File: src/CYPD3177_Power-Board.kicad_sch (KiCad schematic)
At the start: 0 parts

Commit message: Add: Initialized schematic, used the Infineon-CY4533_Guide-UserManual as a guide
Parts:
- added C1, C2, C6, C7: 1µF, symbol Device:C
- added C10: 4.7nF, symbol Device:C
- added C3, C4: 0.1µF, symbol Device:C
- added C5: 3.3µF, symbol Device:C
- added C8, C9: 390pF, symbol Device:C
- added D1: NZH10C,115, symbol Device:D_Zener
- added D2: LTST-C190GKT, symbol Device:LED
- added D3: LED, symbol Device:LED
- added J1: Conn_01x06_Pin, symbol Connector:Conn_01x06_Pin
- added J2: USB4125-GF-A, Connectors_User:GCT_USB4125-GF-A, symbol Connector_User:USB4125-GF-A
- added J3: Conn_01x10_Pin, symbol Connector:Conn_01x10_Pin
- added Q1: IRF9358PbF, Package_SO:HSOP-8-1EP_3.9x4.9mm_P1.27mm_EP2.41x3.1mm_ThermalVias, symbol Transistor_FET_User:IRF9358PBF
- added Q2: BSL308PE, Package_TO_SOT_SMD:SOT-23-6_Handsoldering, symbol Transistor_FET_User:BSL308PE
- added Q3: NTR4503N, symbol Simulation_SPICE:NMOS
- added R1, R5: 49.9kΩ, symbol Device:R
- added R10, R11, R12, R9: 2kΩ, symbol Device:R
- added R13, R4, R7: 1kΩ, symbol Device:R
- added R14: 100kΩ, symbol Device:R
- added R15: 0kΩ, symbol Device:R
- added R16: 5.1Ω, symbol Device:R
- added R17, R19, R20, R21: 5.1kΩ, symbol Device:R
- added R18, R22, R3: 0Ω, symbol Device:R
- added R2: 10kΩ, symbol Device:R
- added R6: 2.2kΩ, symbol Device:R
- added R8: 1M, symbol Device:R
- added U1: CYPD3177-24LQXQx, Package_DFN_QFN:QFN-24-1EP_4x4mm_P0.5mm_EP2.7x2.7mm_ThermalVias, symbol Interface_USB_User:CYPD3177-24LQXQx
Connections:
- new net: Q2.1, Q2.3, R5.2, R7.1
- new net: R7.2, U1.4 (SAFE_PWR_EN)
- new net: J3.6 (Pin_6), R11.2, U1.7 (HPI_INT)
- new net: D2.2 (A), R6.2
- new net: R15.2, R16.1, U1.2 (VBUS_MAX)
- new net: C6.2, C7.2, R2.2, R3.2, R4.1
- new net: Q2.4, Q2.5
- new net: C10.1, J2.S1 (SHIELD), R8.1
- new net: R17.2, R18.1, U1.1 (VBUS_MIN)
- new net: J3.9 (Pin_9), R9.2, U1.10 (FLIP)
- new net: C9.1, J2.B5 (CC2), U1.14 (CC2)
- new net: Q3.1 (D), R13.2
- new net: J3.10 (Pin_10), Q3.2 (G), R14.1, U1.9 (FAULT)
- new net: C8.1, J2.A5 (CC1), U1.15 (CC1)
- new net: J3.5 (Pin_5), R12.2, U1.12 (HPI_SDA)
- new net: R19.2, R20.1, U1.5 (ISNK_COARSE)
- new net: D3.1 (K), R13.1
- new net: J3.4 (Pin_4), U1.13 (HPI_SCL)
- new net: R4.2, U1.3 (VBUS_FET_EN)
- new net: R21.2, R22.1, U1.6 (ISNK_FINE)
- new net: J3.7 (Pin_7), R10.2, U1.8 (GPIO_1)
- new net +1V8: C1.1, J3.2 (Pin_2), U1.24 (VCCD)
- new net +3V3: C2.1, C3.1, C4.1, J3.1 (Pin_1), R10.1, R11.1, R12.1, R15.1, R17.1, R19.1, R21.1, R9.1, U1.23 (VDDD)
- new net 5V_{OUT}: J1.3 (Pin_3), J1.4 (Pin_4), Q2.2
- new net DC_{OUT}: C7.1, D3.2 (A), J1.1 (Pin_1), J1.2 (Pin_2), J3.8 (Pin_8), Q1.3, U1.11 (VDC_OUT)
- new net FET_{Gate}: D1.2 (A), Q1.2, Q1.4, R1.2, R3.1
- new net FET_{SRC}: D1.1 (K), Q1.1, Q1.5, Q1.6, R1.1
- new net GND: C1.2, C10.2, C2.2, C3.2, C4.2, C5.2, C8.2, C9.2, D2.1 (K), J1.5 (Pin_5), J1.6 (Pin_6), J2.A12 (GND), J2.B12 (GND), J3.3 (Pin_3), Q3.3 (S), R14.2, R16.2, R18.2, R20.2, R22.2, R8.2, U1.19 (GND), U1.22 (VSS), U1.25 (EPAD)
- new net VBUS: C5.1, C6.1, J2.A9 (VBUS), J2.B9 (VBUS), Q1.7, Q1.8, Q2.6, R2.1, R5.1, R6.1, U1.18 (VBUS_IN)
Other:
- note added: "I_{Sink, Coarse}"
- note added: "I_{Sink, Fine}"
- note added: "VBUS_{MAX}"
- note added: "VBUS_{MIN}"
- title: <Default Template> -> CYPD3177_Power-Board

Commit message: Mod: Schematic, modified some resistor value to not use as much; Add: Description texts and tables
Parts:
- removed J3: Conn_01x10_Pin, symbol Connector:Conn_01x10_Pin
- added J3, J4, J5: Conn_01x03, symbol Connector_Generic:Conn_01x03
- R10, R11, R12, R9: value 2kΩ -> 2.2kΩ
- R15: value 0kΩ -> 5.1kΩ
- R18, R22: value 0Ω -> 2.2kΩ
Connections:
- net +1V8: now also J3.2 (Pin_2)
- net +3V3: now also J3.1 (Pin_1)
- net DC_{OUT}: no longer D3.2 (A)
- net GND: now also J3.3 (Pin_3)
- net VBUS: now also D3.2 (A)
- net ~{INT}: now reaches R11.2, U1.7 (HPI_INT)
- net ~{INT}: now also J4.3 (Pin_3)
- net VBUS_{MAX}: now reaches R15.2, R16.1, U1.2 (VBUS_MAX)
- net VBUS_{MIN}: now reaches R17.2, R18.1, U1.1 (VBUS_MIN)
- net FLIP: now reaches R9.2, U1.10 (FLIP)
- net FLIP: now also J5.2 (Pin_2)
- net CC2: now reaches C9.1, J2.B5 (CC2), U1.14 (CC2)
- net FAULT: now reaches Q3.2 (G), R14.1, U1.9 (FAULT)
- net FAULT: now also J5.3 (Pin_3)
- net CC1: now reaches C8.1, J2.A5 (CC1), U1.15 (CC1)
- net SDA: now reaches R12.2, U1.12 (HPI_SDA)
- net SDA: now also J4.2 (Pin_2)
- net I_{Sink, Coarse}: now reaches R19.2, R20.1, U1.5 (ISNK_COARSE)
- net SCL: now reaches U1.13 (HPI_SCL)
- net SCL: now also J4.1 (Pin_1)
- net I_{Sink, Fine}: now reaches R21.2, R22.1, U1.6 (ISNK_FINE)
- net GPIO: now reaches R10.2, U1.8 (GPIO_1)
- net GPIO: now also J5.1 (Pin_1)
- net 5V_{OUT} renamed Safe-5V_{OUT}
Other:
- note added: "* When pullup-pulldown combination is 0-none or none-0, use any resistor instead of 0-ohm"
- note added: "+3V3 Ratio"
- note added: "0.25A"
- note added: "0.5A"
- note added: "0.75A"
- note added: "0.9A"
- note added: "0/6"
- note added: "0A"
- note added: "0kΩ*"
- note added: "1/6"
- note added: "10kΩ"
- note added: "12V"
- note added: "15V"
- note added: "19V"
- note added: "1A"
- note added: "1kΩ"
- note added: "2.4kΩ"
- note added: "2/6"
- note added: "20V"
- note added: "2A"
- note added: "3/6"
- note added: "3A"
- note added: "4/6"
- note added: "4A"
- note added: "5.1kΩ"
- note added: "5A"
- note added: "5V"
- note added: "9V"
- note added: ">5/6"
- note added: "Coarse Current"
- note added: "Fine Current"
- note added: "Pull-Down"
- note added: "Pull-Up"
- note added: "Req. Voltage"
- note added: "open"
- moved on the sheet: D2, D3, Q3, R10, R13, R14, R9

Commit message: Mod: Power connector and changed date
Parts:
- removed J1: Conn_01x06_Pin, symbol Connector:Conn_01x06_Pin
- added J1: Conn_01x06, symbol Connector_Generic:Conn_01x06
- D3: value LED -> RED
- renumbered R15 to R14, R17 to R15, R19 to R16, R21 to R17, R14 to R18, R16 to R19, R18 to R20, R20 to R21
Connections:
- net DC_{OUT}: now also J1.1 (Pin_1), J1.2 (Pin_2)
- net GND: now also J1.5 (Pin_5), J1.6 (Pin_6)
- net Safe-5V_{OUT}: now also J1.3 (Pin_3), J1.4 (Pin_4)
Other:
- note added: "Clamp V_{GS} to 10V absolute"
- moved on the sheet: C5

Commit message: Mod: Assigned all footprints, without the connectors
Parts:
- added C5, C6: 1µF, Capacitor_SMD:C_0402_1005Metric, symbol Device:C
- C1, C2: footprint (none) -> Capacitor_SMD:C_0603_1608Metric
- C10: renamed from C8; footprint (none) -> Capacitor_SMD:C_0603_1608Metric_Pad1.08x0.95mm_HandSolder; now not fitted
- C11: renamed from C9; footprint (none) -> Capacitor_SMD:C_0603_1608Metric_Pad1.08x0.95mm_HandSolder; now not fitted
- C12: renamed from C10; footprint (none) -> Capacitor_SMD:C_0805_2012Metric_Pad1.18x1.45mm_HandSolder
- C3, C4: footprint (none) -> Capacitor_SMD:C_0402_1005Metric
- C7: renamed from C5; value 3.3µF -> 1µF; footprint (none) -> Capacitor_SMD:C_0402_1005Metric
- C8: renamed from C6; footprint (none) -> Capacitor_SMD:C_0402_1005Metric
- C9: renamed from C7; footprint (none) -> Capacitor_SMD:C_0402_1005Metric_Pad0.74x0.62mm_HandSolder; now not fitted
- D1: footprint (none) -> Diode_SMD:D_SOD-123F
- D2: footprint (none) -> LED_SMD:LED_0603_1608Metric_Pad1.05x0.95mm_HandSolder
- D3: value RED -> LTST-C190EKT; footprint (none) -> LED_SMD:LED_0603_1608Metric_Pad1.05x0.95mm_HandSolder
- Q3: footprint (none) -> Package_TO_SOT_SMD:SOT-23-3
- R1, R4, R5, R7: footprint (none) -> Resistor_SMD:R_0402_1005Metric
- R10, R11, R12, R14, R15, R16, R17, R19, R20, R21, R22, R6, R8, R9: footprint (none) -> Resistor_SMD:R_0805_2012Metric_Pad1.20x1.40mm_HandSolder
- R13, R3: footprint (none) -> Resistor_SMD:R_0402_1005Metric_Pad0.72x0.64mm_HandSolder
- R18: value 100kΩ -> 49.9kΩ; footprint (none) -> Resistor_SMD:R_0402_1005Metric_Pad0.72x0.64mm_HandSolder
- R2: footprint (none) -> Resistor_SMD:R_0603_1608Metric
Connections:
- net GND: now also C5.2, C6.2
- net VBUS: now also C5.1, C6.1
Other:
- moved on the sheet: C1, C2, C3, C4, D1, D3, Q3, R1, R13

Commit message: Add: Footprint for the connectors (castellated holes) and mounting holes
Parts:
- added H1, H2: MountingHole, MountingHole:MountingHole_3.2mm_M3, symbol Mechanical:MountingHole
- J1: footprint (none) -> Connector_CastellatedHole_2.54mm_User:CastellatedHole_1x06_P2.54mm_PinHeaders
- J2: footprint Connectors_User:GCT_USB4125-GF-A -> Connector_User:GCT_USB4125-GF-A
- J3, J4, J5: footprint (none) -> Connector_CastellatedHole_2.54mm_User:CastellatedHole_1x03_P2.54mm_PinHeader
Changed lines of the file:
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@@
       (effects (font (size 1.27 1.27)) (justify left))
     )
-    (property "Footprint" "" (at 266.7 121.92 0)
+    (property "Footprint" "Connector_CastellatedHole_2.54mm_User:CastellatedHole_1x03_P2.54mm_PinHeader" (at 266.7 121.92 0)
       (effects (font (size 1.27 1.27)) hide)
     )
@@
       (effects (font (size 1.27 1.27)))
     )
-    (property "Footprint" "Connectors_User:GCT_USB4125-GF-A" (at 50.8 80.01 0)
+    (property "Footprint" "Connector_User:GCT_USB4125-GF-A" (at 50.8 80.01 0)
       (effects (font (size 1.27 1.27)) hide)
     )
@@
       (effects (font (size 1.27 1.27)) (justify left))
     )
-    (property "Footprint" "" (at 266.7 111.76 0)
+    (property "Footprint" "Connector_CastellatedHole_2.54mm_User:CastellatedHole_1x03_P2.54mm_PinHeader" (at 266.7 111.76 0)
       (effects (font (size 1.27 1.27)) hide)
     )
@@
       (effects (font (size 1.27 1.27)) (justify left))
     )
-    (property "Footprint" "" (at 266.7 24.13 0)
+    (property "Footprint" "Connector_CastellatedHole_2.54mm_User:CastellatedHole_1x06_P2.54mm_PinHeaders" (at 266.7 24.13 0)
       (effects (font (size 1.27 1.27)) hide)
     )
@@
   (symbol (lib_id "power:GND") (at 72.39 87.63 0) (unit 1)
     (in_bom yes) (on_board yes) (dnp no) (fields_autoplaced)
-    (property "Reference" "#PWR09" (at 72.39 93.98 0)
+    (property "Reference" "#PWR010" (at 72.39 93.98 0)
       (effects (font (size 1.27 1.27)) hide)
     )
@@
       (project "CYPD3177_Power-Board"
         (path "/bfaac094-0365-40a4-8b7a-d4d62ace544e"
-          (reference "#PWR09") (unit 1)
+          (reference "#PWR010") (unit 1)
         )
       )
@@
       (effects (font (size 1.27 1.27)) (justify left))
     )
-    (property "Footprint" "" (at 266.7 88.9 0)
+    (property "Footprint" "Connector_CastellatedHole_2.54mm_User:CastellatedHole_1x03_P2.54mm_PinHeader" (at 266.7 88.9 0)
       (effects (font (size 1.27 1.27)) hide)
     )
@@
     )
   )
+  (symbol (lib_id "Mechanical:MountingHole") (at 25.4 190.5 0) (unit 1)
+    (in_bom yes) (on_board yes) (dnp no) (fields_autoplaced)
+    (property "Reference" "H2" (at 27.94 189.865 0)
+      (effects (font (size 1.27 1.27)) (justify left))
+    )
+    (property "Value" "MountingHole" (at 27.94 192.405 0)
+      (effects (font (size 1.27 1.27)) (justify left))
+    )
+    (property "Footprint" "MountingHole:MountingHole_3.2mm_M3" (at 25.4 190.5 0)
+      (effects (font (size 1.27 1.27)) hide)
+    )
+    (property "Datasheet" "~" (at 25.4 190.5 0)
+      (effects (font (size 1.27 1.27)) hide)
+    )
+    (instances
+      (project "CYPD3177_Power-Board"
+        (path "/bfaac094-0365-40a4-8b7a-d4d62ace544e"
+          (reference "H2") (unit 1)
+        )
+      )
+    )
+  )
   (symbol (lib_id "Device:R") (at 196.85 142.24 0) (unit 1)
     (in_bom yes) (on_board yes) (dnp no) (fields_autoplaced)
@@
   (symbol (lib_id "power:+3V3") (at 259.08 81.28 0) (unit 1)
     (in_bom yes) (on_board yes) (dnp no)
-    (property "Reference" "#PWR06" (at 259.08 85.09 0)
+    (property "Reference" "#PWR08" (at 259.08 85.09 0)
       (effects (font (size 1.27 1.27)) hide)
     )
@@
       (project "CYPD3177_Power-Board"
         (path "/bfaac094-0365-40a4-8b7a-d4d62ace544e"
-          (reference "#PWR06") (unit 1)
+          (reference "#PWR08") (unit 1)
         )
       )
@@
         (path "/bfaac094-0365-40a4-8b7a-d4d62ace544e"
           (reference "C7") (unit 1)
+        )
+      )
+    )
+  )
+  (symbol (lib_id "Mechanical:MountingHole") (at 25.4 177.8 0) (unit 1)
+    (in_bom yes) (on_board yes) (dnp no) (fields_autoplaced)
+    (property "Reference" "H1" (at 27.94 177.165 0)
+      (effects (font (size 1.27 1.27)) (justify left))
+    )
+    (property "Value" "MountingHole" (at 27.94 179.705 0)
+      (effects (font (size 1.27 1.27)) (justify left))
+    )
+    (property "Footprint" "MountingHole:MountingHole_3.2mm_M3" (at 25.4 177.8 0)
+      (effects (font (size 1.27 1.27)) hide)
+    )
+    (property "Datasheet" "~" (at 25.4 177.8 0)
+      (effects (font (size 1.27 1.27)) hide)
+    )
+    (instances
+      (project "CYPD3177_Power-Board"
+        (path "/bfaac094-0365-40a4-8b7a-d4d62ace544e"
+          (reference "H1") (unit 1)
         )
       )
@@
   (symbol (lib_id "power:+1V8") (at 170.18 81.28 0) (unit 1)
     (in_bom yes) (on_board yes) (dnp no) (fields_autoplaced)
-    (property "Reference" "#PWR010" (at 170.18 85.09 0)
+    (property "Reference" "#PWR07" (at 170.18 85.09 0)
       (effects (font (size 1.27 1.27)) hide)
     )
@@
       (project "CYPD3177_Power-Board"
         (path "/bfaac094-0365-40a4-8b7a-d4d62ace544e"
-          (reference "#PWR010") (unit 1)
+          (reference "#PWR07") (unit 1)
         )
       )
@@
   (symbol (lib_id "power:+1V8") (at 256.54 86.36 0) (unit 1)
     (in_bom yes) (on_board yes) (dnp no) (fields_autoplaced)
-    (property "Reference" "#PWR08" (at 256.54 90.17 0)
+    (property "Reference" "#PWR09" (at 256.54 90.17 0)
       (effects (font (size 1.27 1.27)) hide)
     )
@@
       (project "CYPD3177_Power-Board"
         (path "/bfaac094-0365-40a4-8b7a-d4d62ace544e"
-          (reference "#PWR08") (unit 1)
+          (reference "#PWR09") (unit 1)
         )
       )
@@
   (symbol (lib_id "power:+3V3") (at 167.64 76.2 0) (unit 1)
     (in_bom yes) (on_board yes) (dnp no) (fields_autoplaced)
-    (property "Reference" "#PWR07" (at 167.64 80.01 0)
+    (property "Reference" "#PWR06" (at 167.64 80.01 0)
       (effects (font (size 1.27 1.27)) hide)
     )
@@
       (project "CYPD3177_Power-Board"
         (path "/bfaac094-0365-40a4-8b7a-d4d62ace544e"
-          (reference "#PWR07") (unit 1)
-        )
-      )
+          (reference "#PWR06") (unit 1)
+        )
+      )

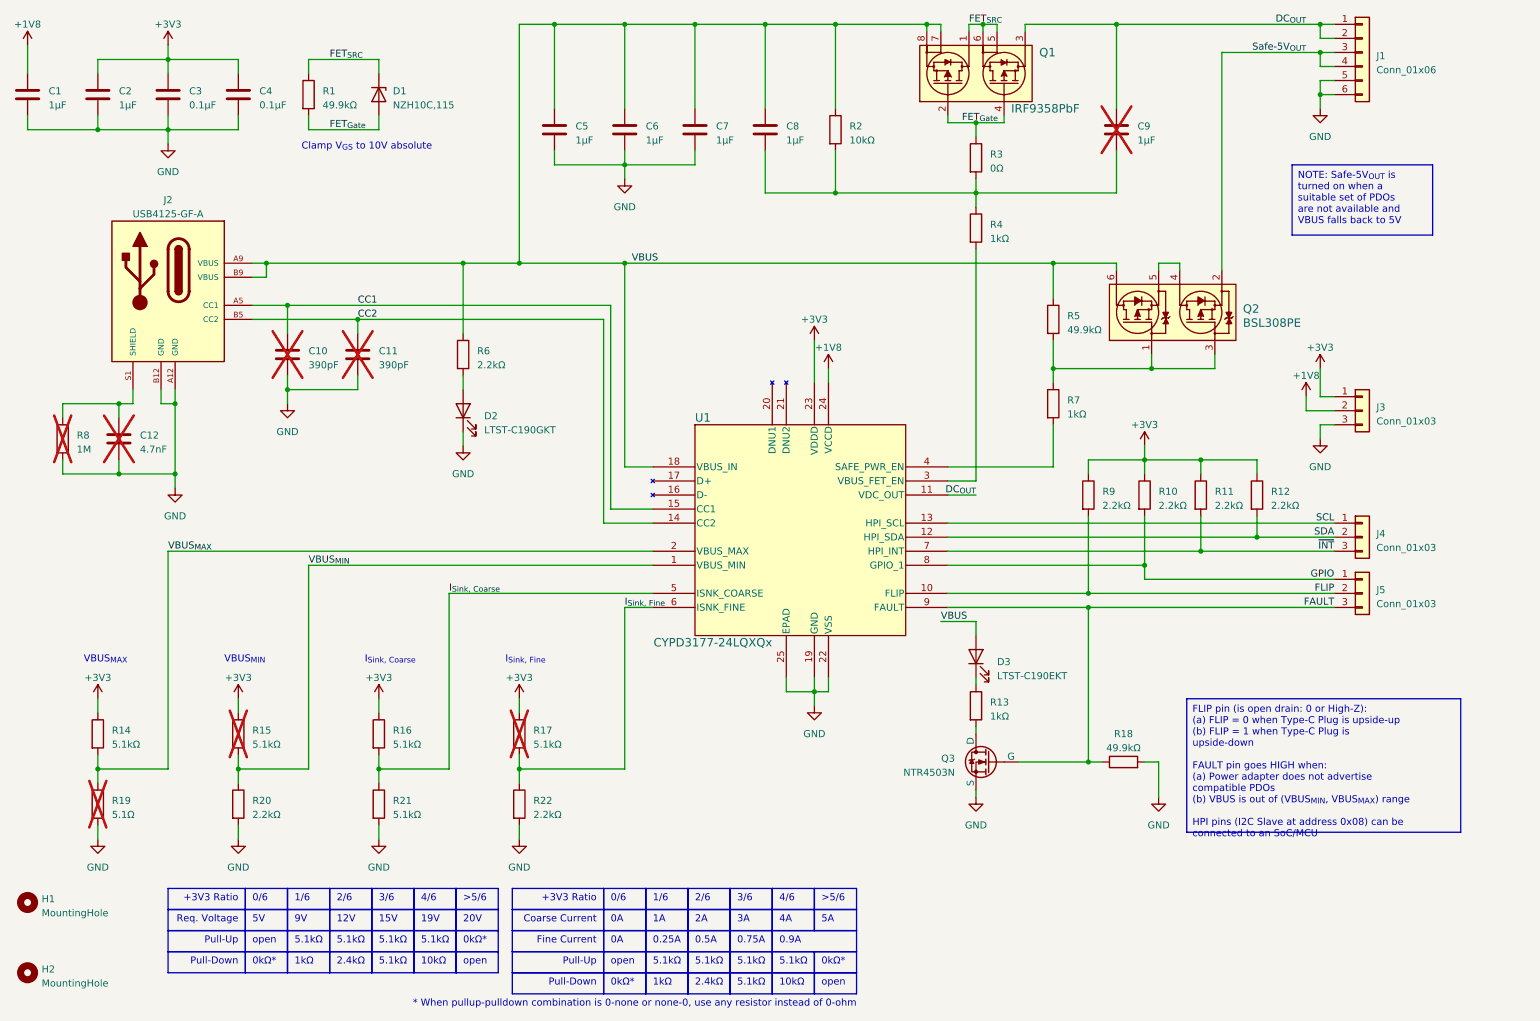
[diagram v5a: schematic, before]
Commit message: Mod: Footpints and changes order of the power outputs on J1
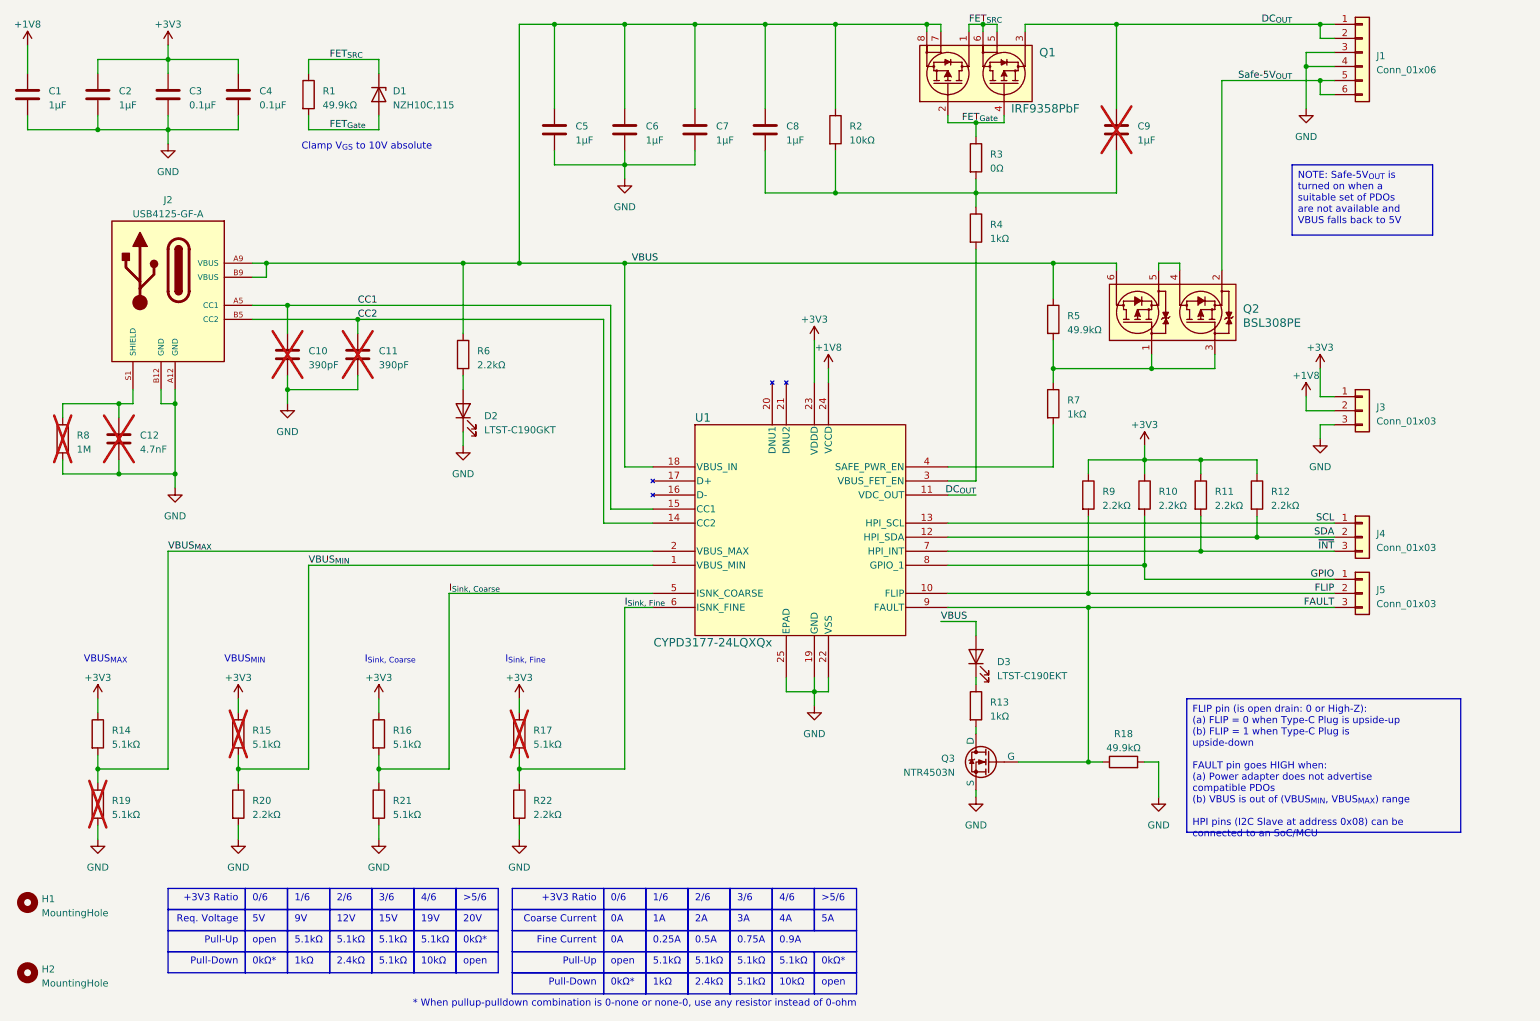
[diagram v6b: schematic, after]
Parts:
- C12: footprint Capacitor_SMD:C_0805_2012Metric_Pad1.18x1.45mm_HandSolder -> Capacitor_SMD:C_0603_1608Metric_Pad1.08x0.95mm_HandSolder
- Q2: footprint Package_TO_SOT_SMD:SOT-23-6_Handsoldering -> Package_TO_SOT_SMD:SOT-23-6
- R19: value 5.1Ω -> 5.1kΩ
- R8: footprint Resistor_SMD:R_0805_2012Metric_Pad1.20x1.40mm_HandSolder -> Resistor_SMD:R_0603_1608Metric_Pad0.98x0.95mm_HandSolder
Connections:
- net GND: now also J1.3 (Pin_3), J1.4 (Pin_4); no longer J1.5 (Pin_5), J1.6 (Pin_6)
- net Safe-5V_{OUT}: now also J1.5 (Pin_5), J1.6 (Pin_6); no longer J1.3 (Pin_3), J1.4 (Pin_4)
